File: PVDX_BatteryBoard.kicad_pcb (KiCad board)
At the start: 2 copper layers, 1 part

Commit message: finished routing
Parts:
- removed REF**: Thermistor_ NXFT15XV103FEAB025, Thermistor_NXFT15XV103FEAB025:Thermistor_ NXFT15XV103FEAB025
- added C1: .1u, Capacitor_SMD:C_0603_1608Metric, F.Cu at (123.1, 51.4)
- added C2: .1u, Capacitor_SMD:C_0603_1608Metric, F.Cu at (122.0, 60.9)
- added C3: .1u, Capacitor_SMD:C_0603_1608Metric, F.Cu at (153.7, 51.3)
- added C4: .1u, Capacitor_SMD:C_0603_1608Metric, F.Cu at (153.2, 61.1)
- added D1: D_Schottky, Diode_SMD:D_SOD-128, F.Cu at (140.8, 141.0)
- added D2: D_Schottky, Diode_SMD:D_SOD-128, F.Cu at (136.8, 141.0)
- added D3: D_Schottky, Diode_SMD:D_SOD-128, F.Cu at (132.7, 141.0)
- added D4: D_Schottky, Diode_SMD:D_SOD-128, F.Cu at (128.7, 141.0)
- added J1: Conn_01x19, Connector_PinHeader_2.54mm:PinHeader_1x19_P2.54mm_Vertical, F.Cu at (113.9, 39.8)
- added J10: Conn_01x02_Pin, Connector_PinSocket_2.54mm:PinSocket_1x02_P2.54mm_Vertical, F.Cu at (106.5, 113.3)
- added J11: Conn_01x01_Pin, Connector_PinSocket_2.54mm:PinSocket_1x01_P2.54mm_Vertical, F.Cu at (174.8, 101.4)
- added J12: Conn_01x02, Connector_PinHeader_2.54mm:PinHeader_1x02_P2.54mm_Vertical, F.Cu at (107.2, 39.7)
- added J2: Conn_01x06, Connector_PinSocket_2.54mm:PinSocket_1x06_P2.54mm_Vertical, F.Cu at (163.4, 39.8)
- added J3: Conn_01x10, Connector_PinSocket_2.54mm:PinSocket_1x10_P2.54mm_Vertical, F.Cu at (127.2, 148.1)
- added J4: Conn_01x02_Pin, Connector_PinSocket_2.54mm:PinSocket_1x02_P2.54mm_Vertical, F.Cu at (106.7, 84.2)
- added J5: Conn_01x01_Pin, Connector_PinSocket_2.54mm:PinSocket_1x01_P2.54mm_Vertical, F.Cu at (174.8, 87.6)
- added J6: Conn_01x02_Pin, Connector_PinSocket_2.54mm:PinSocket_1x02_P2.54mm_Vertical, F.Cu at (106.5, 94.2)
- added J7: Conn_01x01_Pin, Connector_PinSocket_2.54mm:PinSocket_1x01_P2.54mm_Vertical, F.Cu at (174.8, 92.2)
- added J8: Conn_01x02_Pin, Connector_PinSocket_2.54mm:PinSocket_1x02_P2.54mm_Vertical, F.Cu at (106.5, 103.0)
- added J9: Conn_01x01_Pin, Connector_PinSocket_2.54mm:PinSocket_1x01_P2.54mm_Vertical, F.Cu at (174.8, 96.8)
- added Q1: DMC2053UVT, Package_TO_SOT_SMD:TSOT-23-6, F.Cu at (125.7, 77.3)
- added Q2: DMC2053UVT, Package_TO_SOT_SMD:TSOT-23-6, F.Cu at (157.7, 77.1)
- added R1: 10k, Resistor_SMD:R_0603_1608Metric, F.Cu at (125.0, 74.7)
- added R10: 10k, Resistor_SMD:R_0603_1608Metric, F.Cu at (146.3, 75.8)
- added R2: 10k, Resistor_SMD:R_0603_1608Metric, F.Cu at (128.9, 77.2)
- added R3: Heater, Connector_PinHeader_2.54mm:PinHeader_1x02_P2.54mm_Vertical, F.Cu at (117.5, 77.3)
- added R4: 10k, Resistor_SMD:R_0603_1608Metric, F.Cu at (114.8, 76.3)
- added R5: Heater, Connector_PinHeader_2.54mm:PinHeader_1x02_P2.54mm_Vertical, F.Cu at (121.4, 77.3)
- added R6: 10k, Resistor_SMD:R_0603_1608Metric, F.Cu at (156.6, 74.5)
- added R7: 10k, Resistor_SMD:R_0603_1608Metric, F.Cu at (161.0, 77.1)
- added R8: Heater, Connector_PinHeader_2.54mm:PinHeader_1x02_P2.54mm_Vertical, F.Cu at (153.1, 77.1)
- added R9: Heater, Connector_PinHeader_2.54mm:PinHeader_1x02_P2.54mm_Vertical, F.Cu at (149.1, 77.1)
- added Rt1: 15.8k, Resistor_SMD:R_0603_1608Metric, F.Cu at (126.3, 51.4)
- added Rt2: 5.83k, Resistor_SMD:R_0603_1608Metric, F.Cu at (126.3, 53.0)
- added Rt3: 15.8k, Resistor_SMD:R_0603_1608Metric, F.Cu at (125.4, 61.0)
- added Rt4: 5.83k, Resistor_SMD:R_0603_1608Metric, F.Cu at (125.4, 62.8)
- added Rt5: 15.8k, Resistor_SMD:R_0603_1608Metric, F.Cu at (157.3, 51.3)
- added Rt6: 5.83k, Resistor_SMD:R_0603_1608Metric, F.Cu at (157.3, 53.2)
- added Rt7: 15.8k, Resistor_SMD:R_0603_1608Metric, F.Cu at (156.5, 61.1)
- added Rt8: 5.83k, Resistor_SMD:R_0603_1608Metric, F.Cu at (156.5, 62.8)
- added TH1: GA10K3A1IA, Connector_PinHeader_2.54mm:PinHeader_1x02_P2.54mm_Vertical, F.Cu at (122.8, 54.1)
- added TH2: GA10K3A1IA, Connector_PinHeader_2.54mm:PinHeader_1x02_P2.54mm_Vertical, F.Cu at (121.8, 63.8)
- added TH3: GA10K3A1IA, Connector_PinHeader_2.54mm:PinHeader_1x02_P2.54mm_Vertical, F.Cu at (153.4, 54.2)
- added TH4: GA10K3A1IA, Connector_PinHeader_2.54mm:PinHeader_1x02_P2.54mm_Vertical, F.Cu at (153.0, 63.8)
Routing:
- net SOLAR_1s_GND: track 0.00 -> 337.4 mm, vias 0 -> 10
- net BATT4-: track 0.00 -> 124.2 mm, vias 0 -> 1
- net BATT4+: track 0.00 -> 122.2 mm, vias 0 -> 1
- net SOLAR: track 0.00 -> 112.9 mm, vias 0 -> 1
- net BATT2M: track 0.00 -> 112.6 mm, vias 0 -> 1
- net BATT3-: track 0.00 -> 103.5 mm, vias 0 -> 1
- net BATT3+: track 0.00 -> 100.1 mm, vias 0 -> 2
- net BATT1M: track 0.00 -> 92.5 mm, vias 0 -> 1
- net NTC2: track 0.00 -> 90.1 mm, vias 0 -> 2
- net +5V: track 0.00 -> 87.5 mm, vias 0 -> 5
- net BATT3M: track 0.00 -> 87.3 mm, vias 0 -> 1
- net NTC1: track 0.00 -> 81.4 mm, vias 0 -> 2
- net BATT4M: track 0.00 -> 81.4 mm, vias 0 -> 1
- net CHG_OUT: track 0.00 -> 75.8 mm, vias 0 -> 1
- net BATT1+: track 0.00 -> 74.8 mm, vias 0 -> 1
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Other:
- board outline added: 75.7 x 115 mm

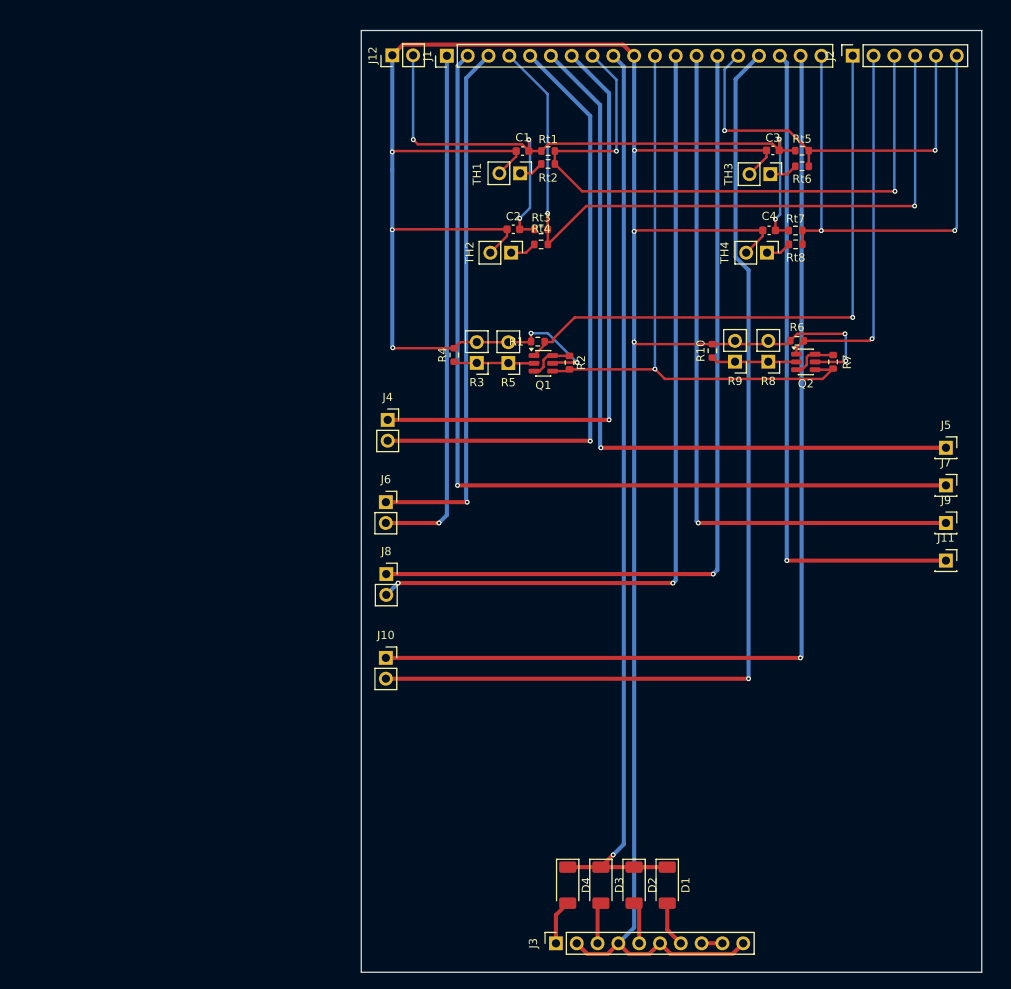
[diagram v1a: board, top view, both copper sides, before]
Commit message: Add screw holes, make battery pack mid 2 holes
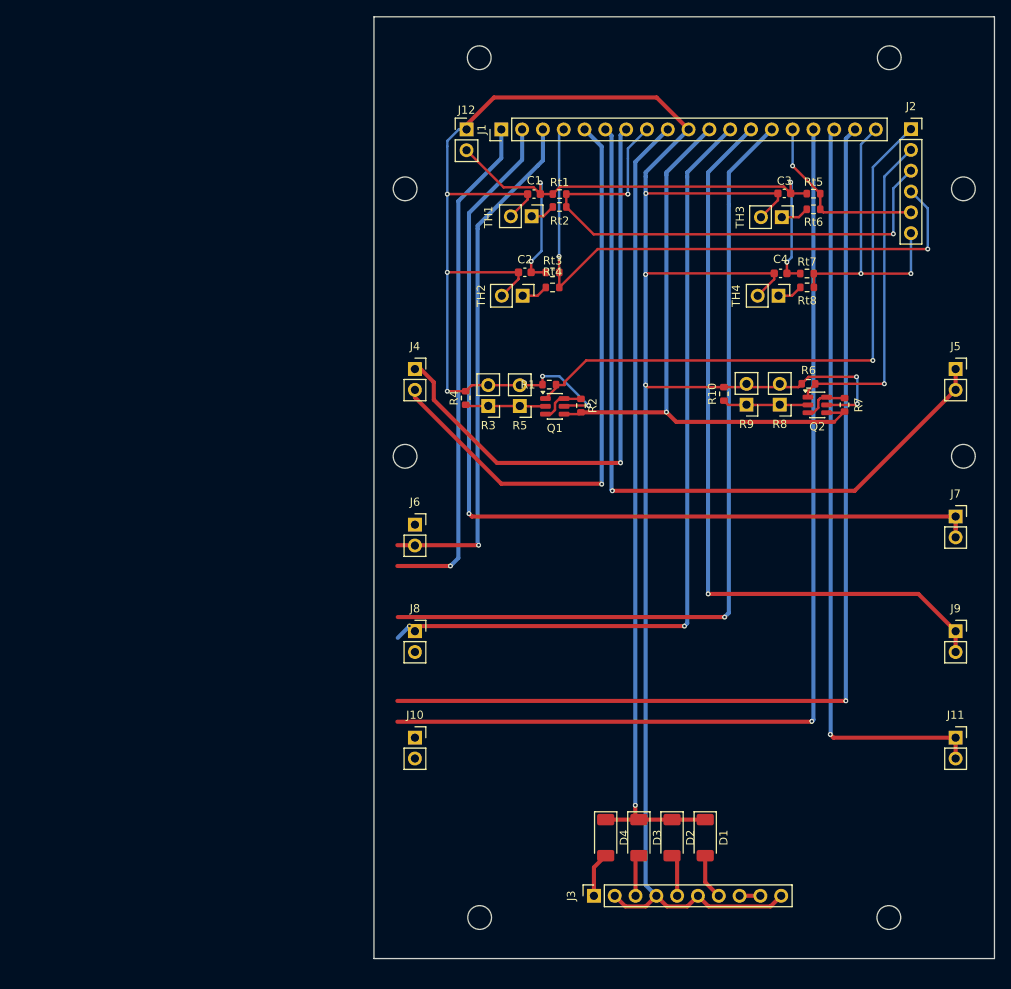
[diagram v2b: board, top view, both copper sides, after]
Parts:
- J11, J5, J7, J9: value Conn_01x01_Pin -> Conn_01x02_Pin; footprint Connector_PinSocket_2.54mm:PinSocket_1x01_P2.54mm_Vertical -> Connector_PinSocket_2.54mm:PinSocket_1x02_P2.54mm_Vertical
- moved J11 21.7 mm to (176.0, 123.0)
- moved J9 13.3 mm to (176.0, 110.0)
- moved J12 12.8 mm to (116.3, 48.8), turned to 0 degrees
- moved J2 11.4 mm to (170.6, 48.7), turned to 0 degrees
- moved J1 11.2 mm to (120.5, 48.8)
- moved J10 10.4 mm to (110.0, 123.0)
- moved J5 9.68 mm to (176.0, 78.0)
- moved J8 7.80 mm to (110.0, 110.0)
- moved D3 7.42 mm to (137.3, 135.2)
- moved D1 7.42 mm to (145.4, 135.2)
- moved D2 7.42 mm to (141.4, 135.2)
- moved D4 7.42 mm to (133.3, 135.2)
- moved J3 7.42 mm to (131.8, 142.3)
- moved J4 7.04 mm to (110.0, 78.0)
- moved Rt4 5.43 mm to (126.8, 68.0)
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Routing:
- net SOLAR_1s_GND: track 337.4 -> 306.3 mm
- net NTC3: track 50.1 -> 22.4 mm, vias 2 -> 1
- net NTC4: track 63.1 -> 36.8 mm
- net NTC2: track 90.1 -> 74.3 mm
- net SOLAR: track 112.9 -> 98.2 mm
- net +5V: track 87.5 -> 73.8 mm, vias 5 -> 4
- net NTC1: track 81.4 -> 67.9 mm
- net BATT4M: track 81.4 -> 92.1 mm
- net BATT3M: track 87.3 -> 93.5 mm
- net HEATER_ON_2: track 45.1 -> 40.3 mm
- net BATT1+: track 74.8 -> 72.3 mm
- net CHG_OUT: track 75.8 -> 74.3 mm
- net BATT3+: track 100.1 -> 98.5 mm
- net BATT2-: track 65.6 -> 64.0 mm
- net BATT3-: track 103.5 -> 101.9 mm
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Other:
- outline, holes or cut-outs redrawn

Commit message: Fix routing, regenerate gerbers
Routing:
- net BATT2+: track 62.3 -> 57.2 mm
- net BATT2-: track 64.0 -> 60.5 mm
- net BATT1+: track 72.3 -> 70.1 mm
- net BATT3M: track 93.5 -> 91.6 mm
- net BATT1M: track 94.0 -> 92.7 mm
- net BATT3+: track 98.5 -> 97.3 mm, vias 2 -> 1
- net BATT3-: track 101.9 -> 100.8 mm
